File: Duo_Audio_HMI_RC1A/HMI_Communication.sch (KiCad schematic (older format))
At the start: 23 parts, among them Q1 BC847, Q2 BC847, U4 SN75176BDR

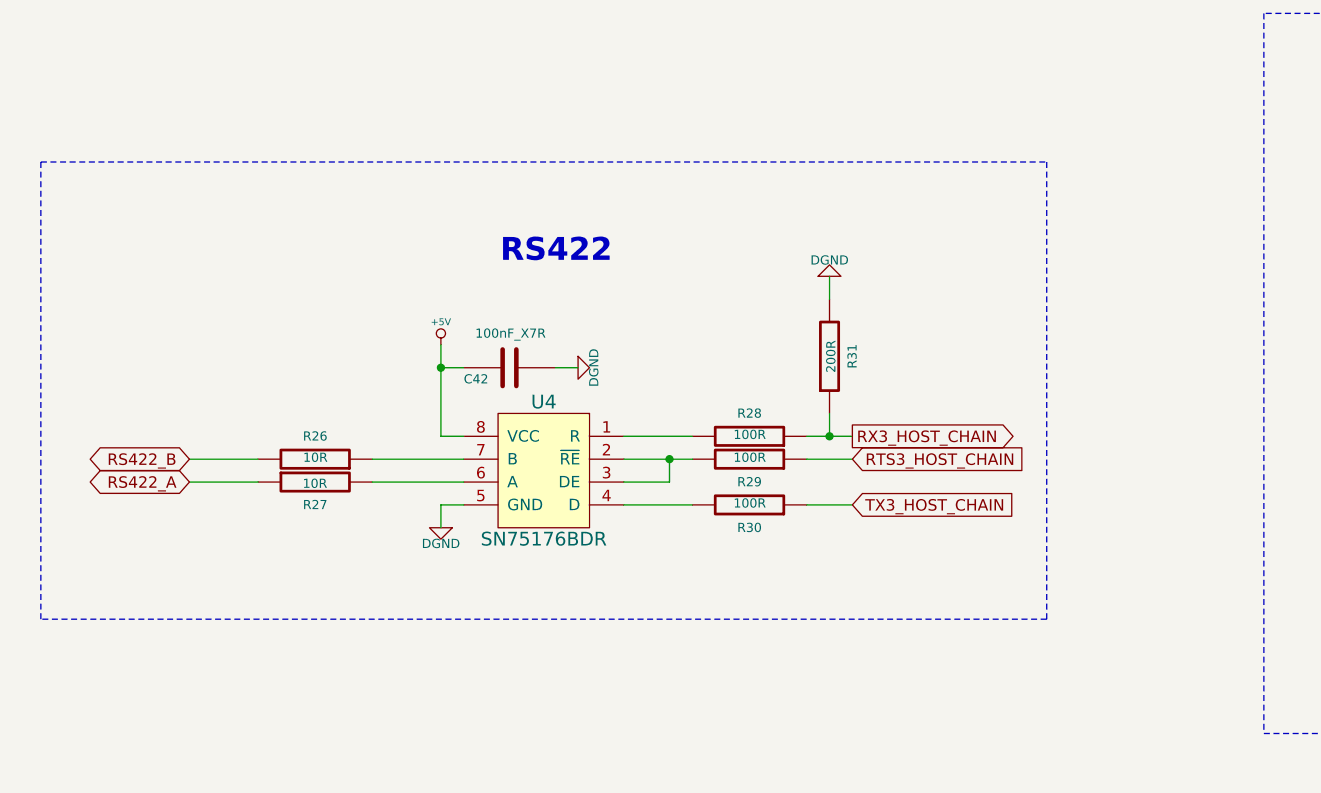
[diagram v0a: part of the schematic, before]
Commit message: Implementing RCA1 schematic  modifications for new layout. Backup commit.
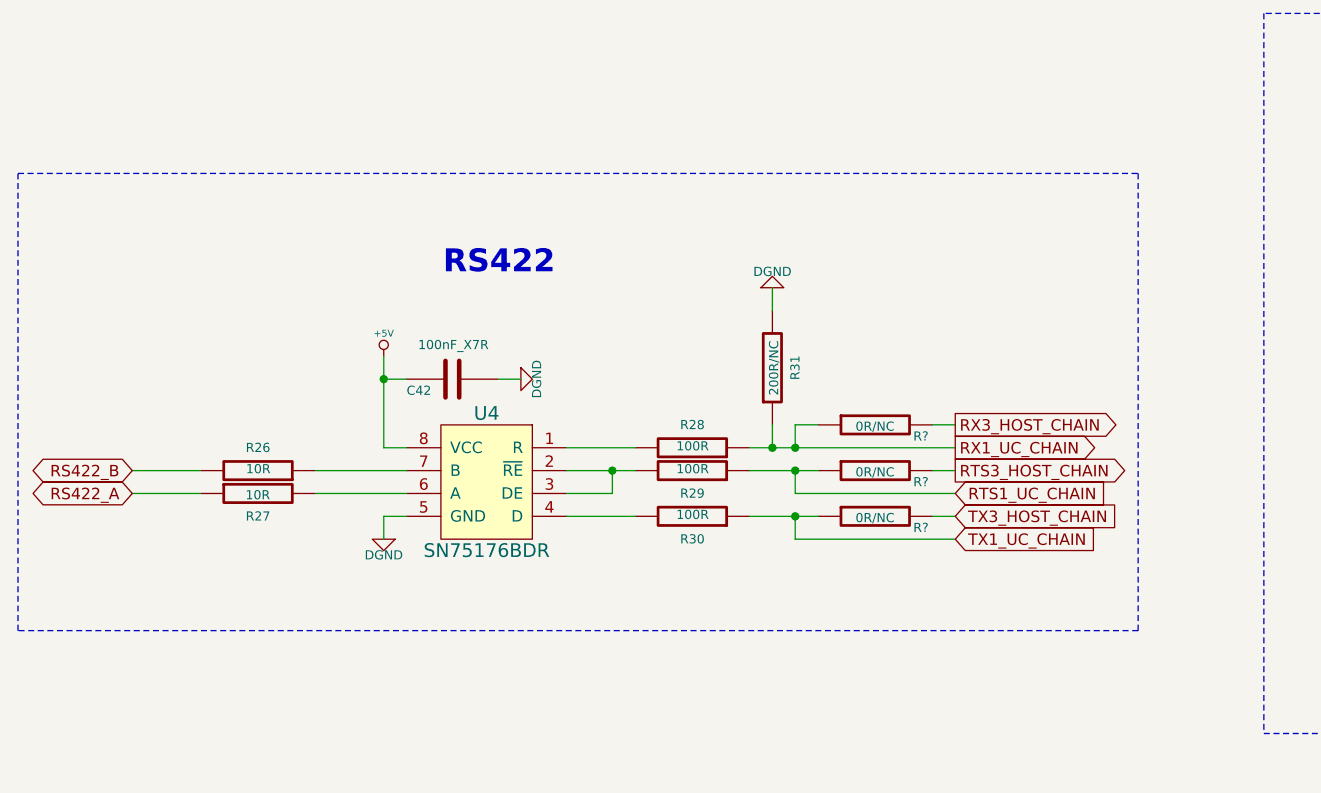
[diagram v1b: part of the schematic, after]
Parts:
- added R? (x3): 0R/NC, SM0603, symbol R
- R31: value 200R -> 200R/NC
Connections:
- net RTS3_HOST_CHAIN: now also R?.2; no longer R29.1
- net RX3_HOST_CHAIN: now also R?.2; no longer R28.1, R31.1
- net TX3_HOST_CHAIN: now also R?.2; no longer R30.1
- new net RTS1_UC_CHAIN: R29.1, R?.1
- new net RX1_UC_CHAIN: R28.1, R31.1, R?.1
- new net TX1_UC_CHAIN: R30.1, R?.1
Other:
- moved on the sheet: C42, R26, R27, R28, R29, R30, R31, U4

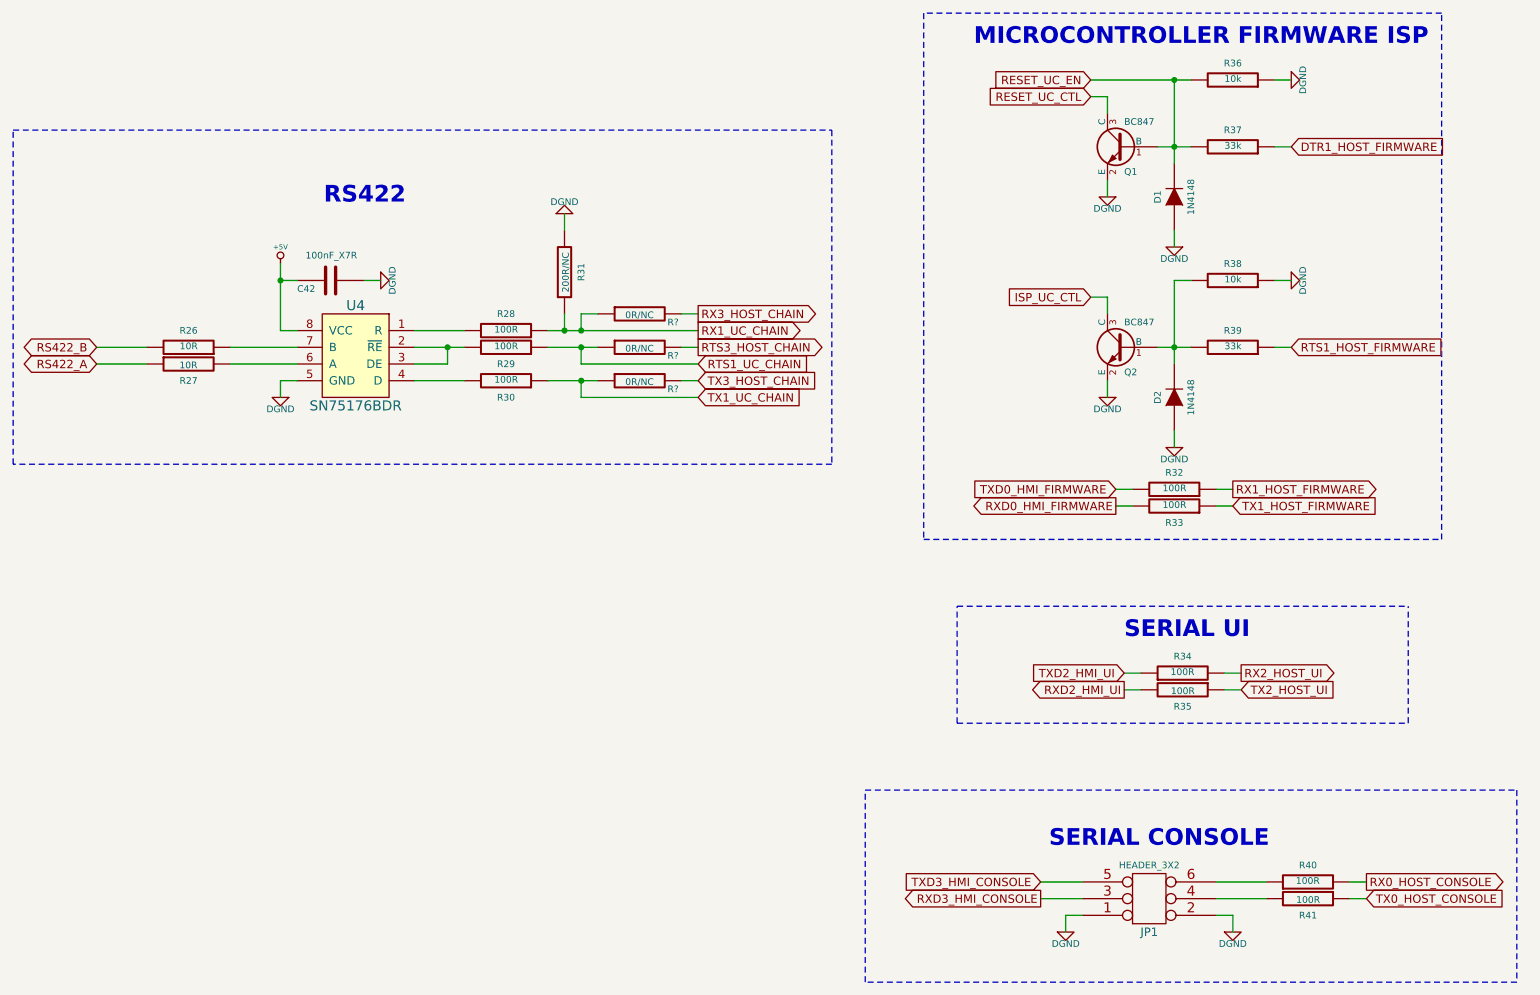
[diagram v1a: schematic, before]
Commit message: Finished RCA1 schematic of the Baseboard and the Pannelboard with USB OTG. Board dimensions, most footprint attribution and major placement implemented in layout. Learning GIT!
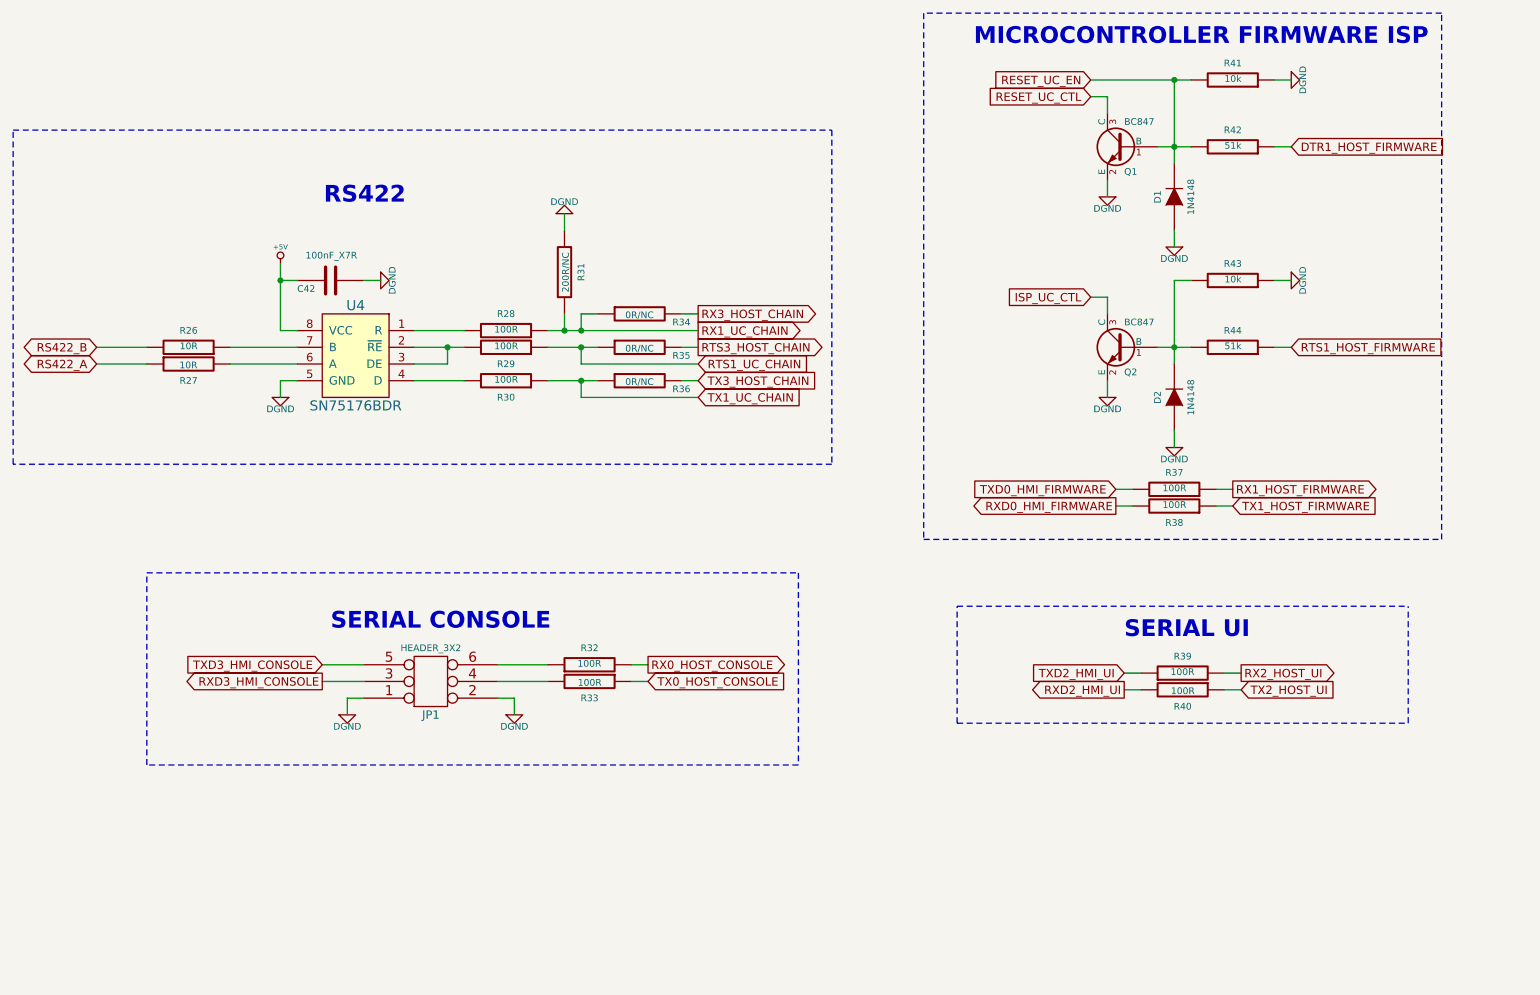
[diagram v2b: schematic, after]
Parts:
- R42: renamed from R37; value 33k -> 51k
- R44: renamed from R39; value 33k -> 51k
- gave numbers to parts that had none: 3
- renumbered R40 to R32, R41 to R33, R32 to R37, R33 to R38, R34 to R39, R35 to R40, R36 to R41, R38 to R43
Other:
- moved on the sheet: JP1, R32, R33
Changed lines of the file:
@@
 LIBS:Duo_Audio_HMI_RC1A
 LIBS:Duo_Audio_HMI_RC1A-cache
-EELAYER 24 0
+EELAYER 27 0
 EELAYER END
 $Descr A4 11693 8268
@@
 Sheet 5 10
 Title "MOD Duo Baseboard RC1A"
-Date "14 may 2014"
+Date "20 may 2014"
 Rev "RC1A"
 Comp ""
@@
 $EndComp
 $Comp
-L DGND #PWR86
+L DGND #PWR085
 U 1 1 532173BF
 P 3400 2500
-F 0 "#PWR86" H 3400 2500 40  0001 C CNN
+F 0 "#PWR085" H 3400 2500 40  0001 C CNN
 F 1 "DGND" H 3400 2430 40  0000 C CNN
 F 2 "~" H 3400 2500 60  0000 C CNN
@@
 $EndComp
 $Comp
-L DGND #PWR85
+L DGND #PWR086
 U 1 1 53217476
 P 2800 3200
-F 0 "#PWR85" H 2800 3200 40  0001 C CNN
+F 0 "#PWR086" H 2800 3200 40  0001 C CNN
 F 1 "DGND" H 2800 3130 40  0000 C CNN
 F 2 "~" H 2800 3200 60  0000 C CNN
@@
 Text Notes 3550 2050 2    100  ~ 20
 RS422
-Text GLabel 7350 6200 0    50   Output ~ 0
+Text GLabel 3050 4900 0    50   Output ~ 0
 RXD3_HMI_CONSOLE
-Text GLabel 7350 6100 0    50   Input ~ 0
+Text GLabel 3050 4800 0    50   Input ~ 0
 TXD3_HMI_CONSOLE
 $Comp
-L R R40
+L R R32
 U 1 1 53219EE6
-P 8950 6100
-F 0 "R40" V 9050 6100 40  0000 C CNN
-F 1 "100R" V 8957 6101 40  0000 C CNN
-F 2 "SM0603" V 8880 6100 30  0001 C CNN
-F 3 "~" H 8950 6100 30  0000 C CNN
-	1    8950 6100
+P 4650 4800
+F 0 "R32" V 4750 4800 40  0000 C CNN
+F 1 "100R" V 4657 4801 40  0000 C CNN
+F 2 "SM0603" V 4580 4800 30  0001 C CNN
+F 3 "~" H 4650 4800 30  0000 C CNN
+	1    4650 4800
 	0    -1   -1   0
 $EndComp
 $Comp
-L R R41
+L R R33
 U 1 1 53219EEC
-P 8950 6200
-F 0 "R41" V 9050 6200 40  0000 C CNN
-F 1 "100R" V 8957 6201 40  0000 C CNN
-F 2 "SM0603" V 8880 6200 30  0001 C CNN
-F 3 "~" H 8950 6200 30  0000 C CNN
-	1    8950 6200
+P 4650 4900
+F 0 "R33" V 4750 4900 40  0000 C CNN
+F 1 "100R" V 4657 4901 40  0000 C CNN
+F 2 "SM0603" V 4580 4900 30  0001 C CNN
+F 3 "~" H 4650 4900 30  0000 C CNN
+	1    4650 4900
 	0    1    1    0
 $EndComp
-Text GLabel 9300 6100 2    50   Output ~ 0
+Text GLabel 5000 4800 2    50   Output ~ 0
 RX0_HOST_CONSOLE
-Text GLabel 9300 6200 2    50   Input ~ 0
+Text GLabel 5000 4900 2    50   Input ~ 0
 TX0_HOST_CONSOLE
 Text GLabel 7850 4950 0    50   Output ~ 0
@@
 TXD2_HMI_UI
 $Comp
-L R R34
+L R R39
 U 1 1 53219EFE
 P 8200 4850
-F 0 "R34" V 8300 4850 40  0000 C CNN
+F 0 "R39" V 8300 4850 40  0000 C CNN
 F 1 "100R" V 8207 4851 40  0000 C CNN
 F 2 "SM0603" V 8130 4850 30  0001 C CNN
@@
 $EndComp
 $Comp
-L R R35
+L R R40
 U 1 1 53219F04
 P 8200 4950
-F 0 "R35" V 8300 4950 40  0000 C CNN
+F 0 "R40" V 8300 4950 40  0000 C CNN
 F 1 "100R" V 8207 4951 40  0000 C CNN
 F 2 "SM0603" V 8130 4950 30  0001 C CNN
@@
 Text Notes 7850 4650 0    100  ~ 20
 SERIAL UI
-Text Notes 7400 5900 0    100  ~ 20
+Text Notes 3100 4600 0    100  ~ 20
 SERIAL CONSOLE
 $Comp
-L DGND #PWR93
+L DGND #PWR087
 U 1 1 5327400C
-P 8500 6400
-F 0 "#PWR93" H 8500 6400 40  0001 C CNN
-F 1 "DGND" H 8500 6330 40  0000 C CNN
-F 2 "~" H 8500 6400 60  0000 C CNN
-F 3 "~" H 8500 6400 60  0000 C CNN
-	1    8500 6400
+P 4200 5100
+F 0 "#PWR087" H 4200 5100 40  0001 C CNN
+F 1 "DGND" H 4200 5030 40  0000 C CNN
+F 2 "~" H 4200 5100 60  0000 C CNN
+F 3 "~" H 4200 5100 60  0000 C CNN
+	1    4200 5100
 	1    0    0    -1
 $EndComp
@@
 TX1_UC_CHAIN
 $Comp
-L R R37
+L R R42
 U 1 1 533FC747
 P 8500 1700
-F 0 "R37" V 8600 1700 40  0000 C CNN
-F 1 "33k" V 8507 1701 40  0000 C CNN
+F 0 "R42" V 8600 1700 40  0000 C CNN
+F 1 "51k" V 8507 1701 40  0000 C CNN
 F 2 "SM0603" V 8430 1700 30  0001 C CNN
 F 3 "~" H 8500 1700 30  0000 C CNN
@@
 $EndComp
 $Comp
-L R R36
+L R R41
 U 1 1 533FC74D
 P 8500 1300
-F 0 "R36" V 8600 1300 40  0000 C CNN
+F 0 "R41" V 8600 1300 40  0000 C CNN
 F 1 "10k" V 8507 1301 40  0000 C CNN
 F 2 "SM0603" V 8430 1300 30  0001 C CNN
@@
 $EndComp
 $Comp
-L DGND #PWR89
+L DGND #PWR088
 U 1 1 533FCB26
 P 7750 2000
-F 0 "#PWR89" H 7750 2000 40  0001 C CNN
+F 0 "#PWR088" H 7750 2000 40  0001 C CNN
 F 1 "DGND" H 7750 1930 40  0000 C CNN
 F 2 "~" H 7750 2000 60  0000 C CNN
@@
 $EndComp
 $Comp
-L DGND #PWR94
+L DGND #PWR089
 U 1 1 533FCF2E
 P 8850 1300
-F 0 "#PWR94" H 8850 1300 40  0001 C CNN
+F 0 "#PWR089" H 8850 1300 40  0001 C CNN
 F 1 "DGND" H 8850 1230 40  0000 C CNN
 F 2 "~" H 8850 1300 60  0000 C CNN
@@
 $EndComp
 $Comp
-L DGND #PWR91
+L DGND #PWR090
 U 1 1 533FE206
 P 8150 2300
-F 0 "#PWR91" H 8150 2300 40  0001 C CNN
+F 0 "#PWR090" H 8150 2300 40  0001 C CNN
 F 1 "DGND" H 8150 2230 40  0000 C CNN
 F 2 "~" H 8150 2300 60  0000 C CNN
@@
 	2800 3100 2800 3200
 Wire Wire Line
-	8400 6100 8700 6100
-Wire Wire Line
-	8400 6200 8700 6200
+	4100 4800 4400 4800
+Wire Wire Line
+	4100 4900 4400 4900
 Wire Wire Line
 	7850 4850 7950 4850
@@
 	2500 3000 2900 3000
 Wire Wire Line
-	7350 6100 7600 6100
-Wire Wire Line
-	7600 6200 7350 6200
-Wire Wire Line
-	8400 6300 8500 6300
-Wire Wire Line
-	8500 6300 8500 6400
-Wire Wire Line
-	7500 6400 7500 6300
-Wire Wire Line
-	7500 6300 7600 6300
+	3050 4800 3300 4800
+Wire Wire Line
+	3300 4900 3050 4900
+Wire Wire Line
+	4100 5000 4200 5000
+Wire Wire Line
+	4200 5000 4200 5100
+Wire Wire Line
+	3200 5100 3200 5000
+Wire Wire Line
+	3200 5000 3300 5000
 Wire Wire Line
 	2000 2900 1700 2900
@@
 	4400 3100 4700 3100
 Wire Wire Line
-	9200 6100 9300 6100
-Wire Wire Line
-	9200 6200 9300 6200
+	4900 4800 5000 4800
+Wire Wire Line
+	4900 4900 5000 4900
 Wire Wire Line
 	7750 1900 7750 2000
@@
 	8150 2200 8150 2300
 $Comp
-L +5V #PWR84
+L +5V #PWR091
 U 1 1 5340D40A
 P 2800 2400
-F 0 "#PWR84" H 2800 2490 20  0001 C CNN
+F 0 "#PWR091" H 2800 2490 20  0001 C CNN
 F 1 "+5V" H 2800 2500 30  0000 C CNN
 F 2 "" H 2800 2400 60  0000 C CNN
@@
 	6850 4450 9550 4450
 Wire Notes Line
-	6300 5550 10200 5550
-Wire Notes Line
-	10200 5550 10200 6700
-Wire Notes Line
-	10200 6700 6300 6700
-Wire Notes Line
-	6300 6700 6300 5550
+	2000 4250 5900 4250
+Wire Notes Line
+	5900 4250 5900 5400
+Wire Notes Line
+	5900 5400 2000 5400
+Wire Notes Line
+	2000 5400 2000 4250
 $Comp
 L CONN_3X2 JP1
 U 1 1 535C82CD
-P 8000 6150
-F 0 "JP1" H 8000 6400 50  0000 C CNN
-F 1 "HEADER_3X2" H 8000 6000 40  0000 C CNN
-F 2 "PIN_ARRAY_3X2" H 8000 6150 60  0001 C CNN
-F 3 "" H 8000 6150 60  0000 C CNN
-	1    8000 6150
+P 3700 4850
+F 0 "JP1" H 3700 5100 50  0000 C CNN
+F 1 "HEADER_3X2" H 3700 4700 40  0000 C CNN
+F 2 "PIN_ARRAY_3X2" H 3700 4850 60  0001 C CNN
+F 3 "" H 3700 4850 60  0000 C CNN
+	1    3700 4850
 	1    0    0    1
 $EndComp
 $Comp
-L DGND #PWR88
+L DGND #PWR092
 U 1 1 532740E6
-P 7500 6400
-F 0 "#PWR88" H 7500 6400 40  0001 C CNN
-F 1 "DGND" H 7500 6330 40  0000 C CNN
-F 2 "~" H 7500 6400 60  0000 C CNN
-F 3 "~" H 7500 6400 60  0000 C CNN
-	1    7500 6400
+P 3200 5100
+F 0 "#PWR092" H 3200 5100 40  0001 C CNN
+F 1 "DGND" H 3200 5030 40  0000 C CNN
+F 2 "~" H 3200 5100 60  0000 C CNN
+F 3 "~" H 3200 5100 60  0000 C CNN
+	1    3200 5100
 	1    0    0    -1
 $EndComp
@@
 RXD0_HMI_FIRMWARE
 $Comp
-L R R32
+L R R37
 U 1 1 535C9C92
 P 8150 3750
-F 0 "R32" V 8250 3750 40  0000 C CNN
+F 0 "R37" V 8250 3750 40  0000 C CNN
 F 1 "100R" V 8157 3751 40  0000 C CNN
 F 2 "SM0603" V 8080 3750 30  0001 C CNN
@@
 $EndComp
 $Comp
-L R R33
+L R R38
 U 1 1 535C9C98
 P 8150 3850
-F 0 "R33" V 8050 3850 40  0000 C CNN
+F 0 "R38" V 8050 3850 40  0000 C CNN
 F 1 "100R" V 8157 3851 40  0000 C CNN
 F 2 "SM0603" V 8080 3850 30  0001 C CNN
@@
 	8500 3850 8400 3850
 $Comp
-L R R39
+L R R44
 U 1 1 535CA647
 P 8500 2900
-F 0 "R39" V 8600 2900 40  0000 C CNN
-F 1 "33k" V 8507 2901 40  0000 C CNN
+F 0 "R44" V 8600 2900 40  0000 C CNN
+F 1 "51k" V 8507 2901 40  0000 C CNN
 F 2 "SM0603" V 8430 2900 30  0001 C CNN
 F 3 "~" H 8500 2900 30  0000 C CNN
@@
 $EndComp
 $Comp
-L R R38
+L R R43
 U 1 1 535CA64D
 P 8500 2500
-F 0 "R38" V 8600 2500 40  0000 C CNN
+F 0 "R43" V 8600 2500 40  0000 C CNN
 F 1 "10k" V 8507 2501 40  0000 C CNN
 F 2 "SM0603" V 8430 2500 30  0001 C CNN
@@
 $EndComp
 $Comp
-L DGND #PWR90
+L DGND #PWR093
 U 1 1 535CA653
 P 7750 3200
-F 0 "#PWR90" H 7750 3200 40  0001 C CNN
+F 0 "#PWR093" H 7750 3200 40  0001 C CNN
 F 1 "DGND" H 7750 3130 40  0000 C CNN
 F 2 "~" H 7750 3200 60  0000 C CNN
@@
 $EndComp
 $Comp
-L DGND #PWR95
+L DGND #PWR094
 U 1 1 535CA659
 P 8850 2500
-F 0 "#PWR95" H 8850 2500 40  0001 C CNN
+F 0 "#PWR094" H 8850 2500 40  0001 C CNN
 F 1 "DGND" H 8850 2430 40  0000 C CNN
 F 2 "~" H 8850 2500 60  0000 C CNN
@@
 $EndComp
 $Comp
-L DGND #PWR92
+L DGND #PWR095
 U 1 1 535CA668
 P 8150 3500
-F 0 "#PWR92" H 8150 3500 40  0001 C CNN
+F 0 "#PWR095" H 8150 3500 40  0001 C CNN
 F 1 "DGND" H 8150 3430 40  0000 C CNN
 F 2 "~" H 8150 3500 60  0000 C CNN
@@
 $EndComp
 $Comp
-L DGND #PWR87
+L DGND #PWR096
 U 1 1 5373C3D5
 P 4500 2100
-F 0 "#PWR87" H 4500 2100 40  0001 C CNN
+F 0 "#PWR096" H 4500 2100 40  0001 C CNN
 F 1 "DGND" H 4500 2030 40  0000 C CNN
 F 2 "~" H 4500 2100 60  0000 C CNN
@@
 Connection ~ 4500 2800
 $Comp
-L R R?
+L R R34
 U 1 1 537C2686
 P 4950 2700
-F 0 "R?" V 5000 2500 40  0000 C CNN
+F 0 "R34" V 5000 2450 40  0000 C CNN
 F 1 "0R/NC" V 4957 2701 40  0000 C CNN
 F 2 "SM0603" V 4880 2700 30  0001 C CNN
@@
 $EndComp
 $Comp
-L R R?
+L R R35
 U 1 1 537C2691
 P 4950 2900
-F 0 "R?" V 5000 2700 40  0000 C CNN
+F 0 "R35" V 5000 2650 40  0000 C CNN
 F 1 "0R/NC" V 4957 2901 40  0000 C CNN
 F 2 "SM0603" V 4880 2900 30  0001 C CNN
@@
 $EndComp
 $Comp
-L R R?
+L R R36
 U 1 1 537C26A7
 P 4950 3100
-F 0 "R?" V 5000 2900 40  0000 C CNN
+F 0 "R36" V 5000 2850 40  0000 C CNN
 F 1 "0R/NC" V 4957 3101 40  0000 C CNN
 F 2 "SM0603" V 4880 3100 30  0001 C CNN
